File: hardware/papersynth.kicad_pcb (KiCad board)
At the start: 2 copper layers, 200 x 48.5 mm, 106 parts, among them J1 USB_OTG, J2 JACK_2P, J3 Micro_SD_Card_Det, J4 JACK_TRS_5PINS, J5 JACK_2P, Q1 Q_NPN_BEC, Q2 Q_NPN_BEC, SW1 SW_Push, SW2 SW_Push, U1 CP2102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

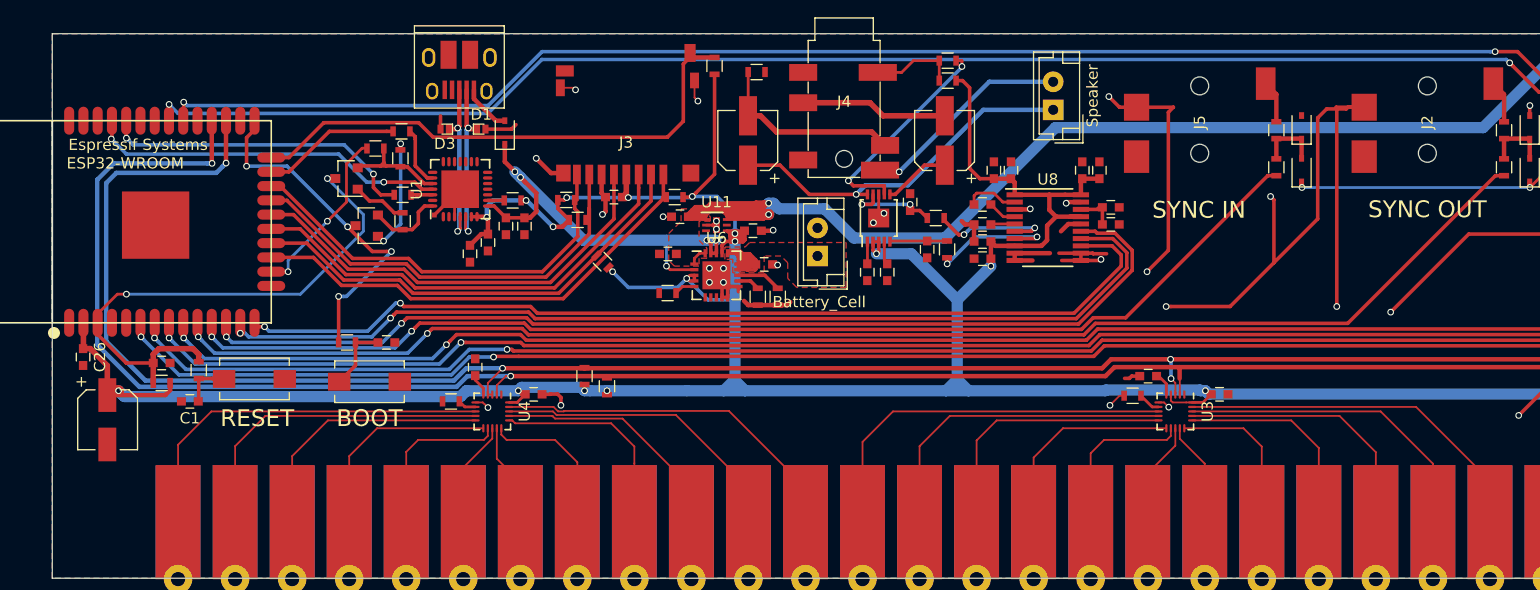
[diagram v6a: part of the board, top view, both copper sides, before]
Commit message: Added solder mask keep out
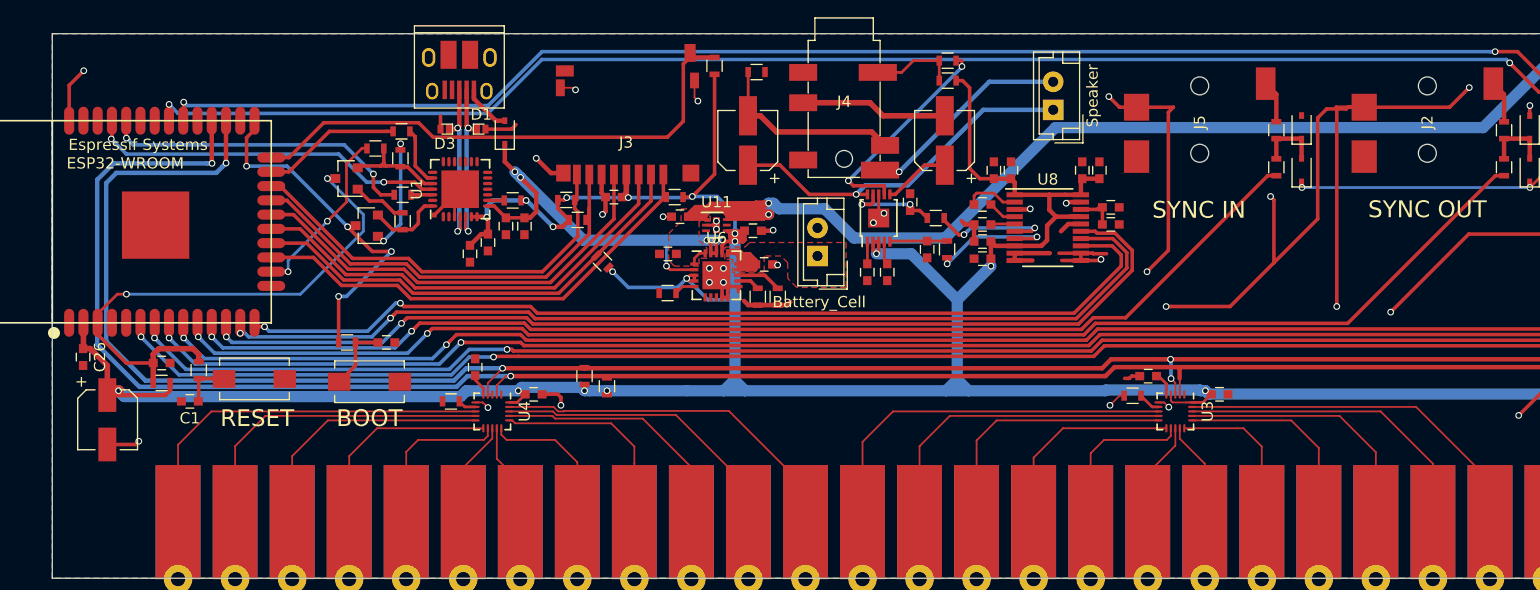
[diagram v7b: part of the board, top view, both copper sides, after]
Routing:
- net GND: track 260.4 -> 278.4 mm, vias 36 -> 39
- net Net-(U4-Pad17): track 22.0 -> 23.0 mm
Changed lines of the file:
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@@
     (thickness 1.6)
     (drawings 8)
-    (tracks 1470)
+    (tracks 1479)
     (zones 0)
     (modules 106)
@@
   (segment (start 129.113 114.7) (end 129.113 115.5205) (width 0.32) (layer F.Cu) (net 1))
   (segment (start 130.6205 115.0205) (end 130.65 115.05) (width 0.32) (layer F.Cu) (net 1))
+  (segment (start 184.843 101.05) (end 192.45 101.05) (width 0.32) (layer F.Cu) (net 2))
+  (segment (start 192.45 101.05) (end 194.2 99.3) (width 0.32) (layer F.Cu) (net 2))
+  (via (at 194.2 99.3) (size 0.6) (drill 0.4) (layers F.Cu B.Cu) (net 2))
+  (segment (start 72.898 131.088) (end 75.412 131.088) (width 0.32) (layer F.Cu) (net 2))
+  (segment (start 75.412 131.088) (end 75.7 130.8) (width 0.32) (layer F.Cu) (net 2))
+  (via (at 75.7 130.8) (size 0.6) (drill 0.4) (layers F.Cu B.Cu) (net 2))
+  (segment (start 69.5 102.25) (end 69.5 99.1) (width 0.32) (layer F.Cu) (net 2))
+  (segment (start 69.5 99.1) (end 70.8 97.8) (width 0.32) (layer F.Cu) (net 2))
+  (via (at 70.8 97.8) (size 0.6) (drill 0.4) (layers F.Cu B.Cu) (net 2))
   (segment (start 217.2875 110.0875) (end 215.5 108.3) (width 0.32) (layer B.Cu) (net 2))
   (segment (start 215.5 108.3) (end 215.5 107.7) (width 0.32) (layer B.Cu) (net 2))
@@
   (segment (start 107.5 102.25) (end 105.55 100.3) (width 0.4) (layer F.Cu) (net 25))
   (segment (start 105.55 100.3) (end 105.55 99.5) (width 0.4) (layer F.Cu) (net 25))
+  (segment (start 104.25 103.05) (end 104.25 111.9) (width 0.4) (layer B.Cu) (net 26))
   (segment (start 103.325 103) (end 104 103) (width 0.4) (layer F.Cu) (net 26))
   (segment (start 104 103) (end 104.1 102.9) (width 0.4) (layer F.Cu) (net 26))
@@
   (via (at 104.1 112.1) (size 0.6) (drill 0.4) (layers F.Cu B.Cu) (net 26))
   (segment (start 104.25 102.75) (end 104.25 99.5) (width 0.4) (layer F.Cu) (net 26))
-  (segment (start 104.25 103.05) (end 104.25 111.9) (width 0.4) (layer B.Cu) (net 26))
   (segment (start 104.1 102.9) (end 104.25 103.05) (width 0.4) (layer B.Cu) (net 26))
   (via (at 104.1 102.9) (size 0.6) (drill 0.4) (layers F.Cu B.Cu) (net 26))
@@
   (segment (start 119.84 131.27) (end 119.84 132.76) (width 0.16) (layer F.Cu) (net 109))
   (segment (start 109.223 129.203) (end 117.773 129.203) (width 0.16) (layer F.Cu) (net 109))
-  (segment (start 124.92 134.92) (end 124.92 138) (width 0.16) (layer F.Cu) (net 110))
-  (segment (start 112.775694 128.780024) (end 118.780024 128.780024) (width 0.16) (layer F.Cu) (net 110))
-  (segment (start 112.588235 128.592565) (end 112.775694 128.780024) (width 0.16) (layer F.Cu) (net 110))
   (segment (start 108.688 128.543) (end 112.538671 128.543) (width 0.16) (layer F.Cu) (net 110))
-  (segment (start 118.780024 128.780024) (end 124.92 134.92) (width 0.16) (layer F.Cu) (net 110))
   (segment (start 112.538671 128.543) (end 112.588235 128.592565) (width 0.16) (layer F.Cu) (net 110))
+  (segment (start 124.92 133.12) (end 124.92 138) (width 0.16) (layer F.Cu) (net 110))
+  (segment (start 112.588235 128.592565) (end 112.775694 128.780024) (width 0.16) (layer F.Cu) (net 110))
+  (segment (start 112.775694 128.780024) (end 120.580024 128.780024) (width 0.16) (layer F.Cu) (net 110))
+  (segment (start 120.580024 128.780024) (end 124.92 133.12) (width 0.16) (layer F.Cu) (net 110))
   (segment (start 130 134.92) (end 130 138) (width 0.16) (layer F.Cu) (net 111))
   (segment (start 112.908246 128.460013) (end 123.540013 128.460013) (width 0.16) (layer F.Cu) (net 111))
@@
       )
     )
+  )
+  (zone (net 1) (net_name +BATT) (layer F.Mask) (hatch edge 0.508)
+    (connect_pads (clearance 0.508))
+    (min_thickness 0.254)
+    (fill yes (arc_segments 16) (thermal_gap 0.508) (thermal_bridge_width 0.508))
+    (polygon
+      (pts
+        (xy 68 143) (xy 268 143) (xy 268 133) (xy 68 133)
+      )
+    )
+  )
+  (zone (net 1) (net_name +BATT) (layer B.Mask) (hatch edge 0.508)
+    (connect_pads (clearance 0.508))
+    (min_thickness 0.254)
+    (fill yes (arc_segments 16) (thermal_gap 0.508) (thermal_bridge_width 0.508))
+    (polygon
+      (pts
+        (xy 68 143) (xy 68 133) (xy 268 133) (xy 268 143)
+      )
+    )

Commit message: Finished routing
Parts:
- moved C35 34.4 mm to (127.5, 76.0)
- moved R15 34.4 mm to (112.6, 89.9)
- moved C26 34.4 mm to (50.7, 95.3)
- moved BT1 34.4 mm to (116.2, 86.3)
- moved C1 34.4 mm to (60.2, 99.2)
- moved C10 34.4 mm to (186.1, 95.3)
- moved C11 34.4 mm to (145.6, 97.0)
- moved C12 34.4 mm to (85.7, 96.2)
- moved C13 34.4 mm to (102.8, 86.1)
- moved C14 34.4 mm to (111.4, 87.0)
- moved C15 34.4 mm to (103.9, 82.8)
- moved C16 34.4 mm to (110.4, 84.0)
- moved C17 34.4 mm to (130.8, 81.7)
- moved C18 34.4 mm to (130.8, 83.5)
- moved C19 34.4 mm to (139.7, 78.7)
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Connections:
- U1 pad 13: Net-(U1-Pad10) -> Net-(U1-Pad13)
- U1 pad 14: Net-(U1-Pad10) -> Net-(U1-Pad14)
- U1 pad 15: Net-(U1-Pad10) -> Net-(U1-Pad15)
- U1 pad 16: Net-(U1-Pad10) -> Net-(U1-Pad16)
- U1 pad 17: Net-(U1-Pad10) -> Net-(U1-Pad17)
- U1 pad 18: Net-(U1-Pad10) -> Net-(U1-Pad18)
- U1 pad 19: Net-(U1-Pad10) -> Net-(U1-Pad19)
- U1 pad 20: Net-(U1-Pad10) -> Net-(U1-Pad20)
- U1 pad 21: Net-(U1-Pad10) -> Net-(U1-Pad21)
- U1 pad 22: Net-(U1-Pad10) -> Net-(U1-Pad22)
- U11 pad 1: VUNREG -> GND
- U11 pad 2: GND -> +3V3
- U11 pad 3: Net-(U11-Pad3) -> +3V3
- U11 pad 4: +3V3 -> VUNREG
- U11 pad 5: Net-(U11-Pad3) -> Net-(U11-Pad5)
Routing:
- net GND: track 278.4 -> 291.1 mm, vias 39 -> 41
- net VUNREG: track 142.3 -> 139.5 mm
- net +3V3: track 402.7 -> 400.0 mm
- removed copper zone on F.Cu, net VUNREG
